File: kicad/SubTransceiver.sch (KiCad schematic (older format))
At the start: 50 parts

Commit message: Adding transceiver
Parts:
- U?: symbol RF_Mixer:ADE-6 -> RCTX-rescue:ADE-6-RF_Mixer
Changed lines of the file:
@@
 	1400 5050 1400 5150
 $Comp
-L RF_Mixer:ADE-6 U?
+L RCTX-rescue:ADE-6-RF_Mixer U?
 U 1 1 5FD5B378
 P 5100 4600

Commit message: New rx-tx bidirectional amplifier
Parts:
- removed C? (x6): 100p, symbol device:C
- removed C? (x4): 1u, symbol device:C
- removed D? (x4): D, symbol device:D
- removed L? (x7): L, symbol device:L
- removed R? (x4): R, symbol device:R
- removed U? (x2): MAX2650, smd-semi:SOT-143, symbol maxim_1:MAX2650
- removed U?: ADE-6, RF_Mini-Circuits:Mini-Circuits_CD542_LandPatternPL-052, symbol RCTX-rescue:ADE-6-RF_Mixer
- added C? (x12): 100p, symbol device:C
- added C? (x6): 1u, symbol device:C
- added L? (x4): L, symbol device:L
- added R? (x4): R, symbol device:R
- added U? (x4): MAR-6SM+, symbol mc-amplifiers:ERA-6+
- added U?: ADE-1+, RF_Mini-Circuits:Mini-Circuits_CD542_LandPatternPL-052, symbol RF_Mixer:ADE-1+
- added U? (x2): TLV70245_SOT23-5, TO_SOT_Packages_SMD:SOT-23-5, symbol regul:TLV70245_SOT23-5
- added U?: LM1117-3.3, symbol regul:LM1117-3.3
- added U? (x4): MAX2650, smd-semi:SOT-143, symbol maxim_1:MAX2650
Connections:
- net labels added: +VRx, +VTx, VCC
- net labels removed: RX_VCC, TX_VCC
- wire segments 127 -> 171
- no-connect marks 1 -> 0
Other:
- moved on the sheet: C?, J?, L?, U?, Y?

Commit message: New rx-tx bidirectional amplifier
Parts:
- removed C? (x16): 100p, symbol device:C
- removed C?: 100n, symbol device:C
- removed C? (x12): 1u, symbol device:C
- removed J?: 50 Ohm Antenna, symbol conn:Conn_Coaxial
- removed L? (x11): L, symbol device:L
- removed R? (x4): R, symbol device:R
- removed U?: Si4464, Package_DFN_QFN:QFN-20-1EP_4x4mm_P0.5mm_EP2.6x2.6mm_ThermalVias, symbol RF:Si4464
- removed U? (x4): MAR-6SM+, symbol mc-amplifiers:ERA-6+
- removed U?: ADE-1+, RF_Mini-Circuits:Mini-Circuits_CD542_LandPatternPL-052, symbol RF_Mixer:ADE-1+
- removed U? (x2): TLV70245_SOT23-5, TO_SOT_Packages_SMD:SOT-23-5, symbol regul:TLV70245_SOT23-5
- removed U?: LM1117-3.3, symbol regul:LM1117-3.3
- removed U? (x4): MAX2650, smd-semi:SOT-143, symbol maxim_1:MAX2650
- removed Y?: 30 MHz, symbol device:Crystal
- removed Y?: Si500D, Si500D, symbol Si500D:Si500D
- added C? (x16): 100p, symbol device:C
- added C?: 100n, symbol device:C
- added C? (x10): 1u, symbol device:C
- added J?: 50 Ohm Antenna, symbol conn:Conn_Coaxial
- added J?: TRANSCEIVER, symbol conn:Conn_01x06
- added L? (x8): L, symbol device:L
- added P?: TX_VCC, Connectors_Samtec:SL-102-X-XX_1x02, symbol RCTX-rescue:Conn_01x02-conn
- added P?: PWR_BUS, Connectors_Samtec:SL-104-X-XX_1x04, symbol RCTX-rescue:Conn_01x04-conn
- added R?: R, symbol device:R
- added U?: Si4464, Package_DFN_QFN:QFN-20-1EP_4x4mm_P0.5mm_EP2.6x2.6mm_ThermalVias, symbol RF:Si4464
- added U? (x2): TLV70245_SOT23-5, TO_SOT_Packages_SMD:SOT-23-5, symbol regul:TLV70245_SOT23-5
- added U? (x4): MAX2650, smd-semi:SOT-143, symbol maxim_1:MAX2650
- added U?: ADE-1+, RF_Mini-Circuits:Mini-Circuits_CD542_LandPatternPL-052, symbol RF_Mixer:ADE-1+
- added Y?: 30 MHz, symbol device:Crystal
- added Y?: Si500D, Si500D, symbol Si500D:Si500D
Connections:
- net labels removed: VCC
- wire segments 171 -> 178
- no-connect marks 0 -> 2
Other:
- note added: "+3.3V"
- note added: "+5V"
- note added: "/IRQ"
- note added: "/SEL"
- note added: "GND"
- note added: "Low pass filter fc: 260 MHz"
- note added: "Low pass filter fc: 80 MHz"
- note added: "PPM"
- note added: "SCLK"
- note added: "SDI"
- note added: "SDO"
- note added: "VBAT+"
- note added: "from Switches module (RF_SWITCH_3P2V)"
- note added: "to Switches module (RF_SWITCH_3P2V)"

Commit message: New rx-tx bidirectional amplifier
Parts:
- removed C? (x4): 100p, symbol device:C
- removed J?: TRANSCEIVER, symbol conn:Conn_01x06
- added C? (x3): 1u, symbol device:C
- added C? (x7): 100p, symbol device:C
- added J?: TRANSCEIVER, symbol conn:Conn_01x07
- added L?: L, symbol device:L
- added R?: R, symbol device:R
- Y?: value Si500D -> Si500DFAD165M000 / Si511NCB165M000C
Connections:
- wire segments 178 -> 204
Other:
- note added: "/RF_EN"
- note added: "Harmonic\ntermination"
- moved on the sheet: C?, J?, L?, P?, R?, U?, Y?

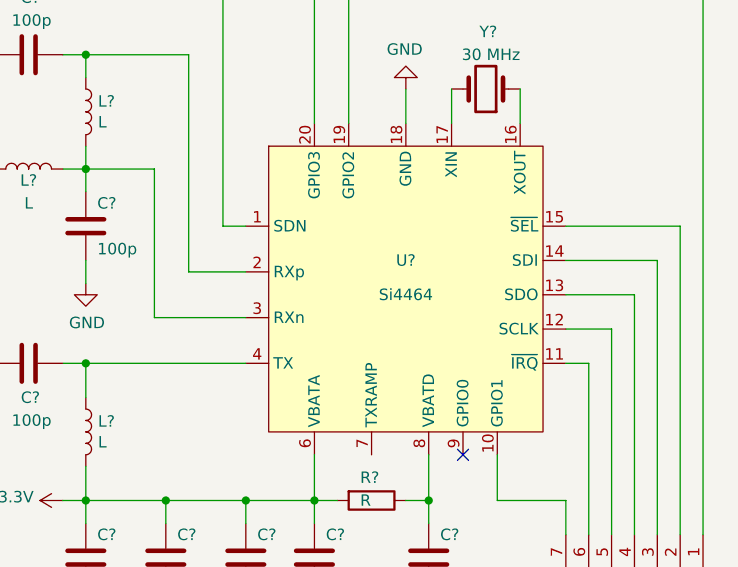
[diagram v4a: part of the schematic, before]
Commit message: Using ERF32FG12 SoC instead of PIC32MX
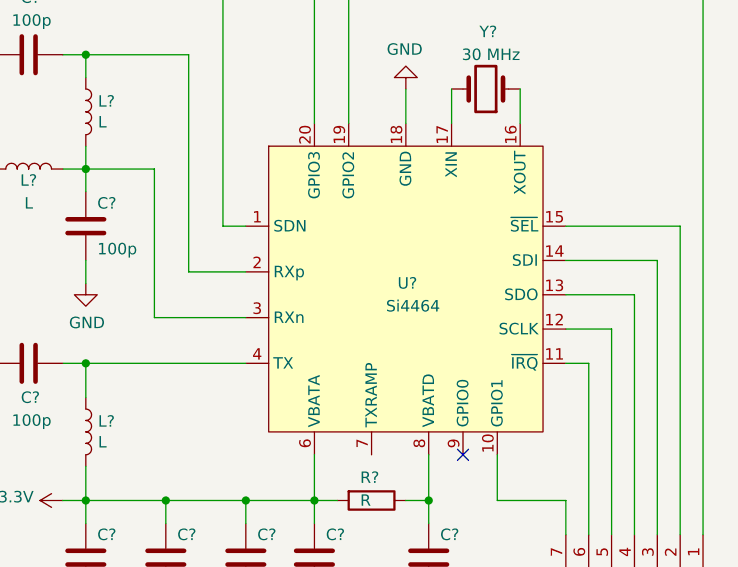
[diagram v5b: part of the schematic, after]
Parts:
- removed U?: Si4464, Package_DFN_QFN:QFN-20-1EP_4x4mm_P0.5mm_EP2.6x2.6mm_ThermalVias, symbol RF:Si4464
- added U?: Si4464, Package_DFN_QFN:QFN-20-1EP_4x4mm_P0.5mm_EP2.6x2.6mm_ThermalVias, symbol RF:Si4464
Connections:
- net +3V3: now also U?.6 (VBATA)
- net GND: now also U?.18 (GND), U?.21 (GND)
- net at C?.1, R?.1: now also U?.8 (VBATD)
- net at J?.1 (Pin_1), Y?.1 (OE): now also U?.1 (SDN)
- net at J?.7 (Pin_7): now also U?.10 (GPIO1)
- net at J?.6 (Pin_6): now also U?.11 (~IRQ)
- net at J?.5 (Pin_5): now also U?.12 (SCLK)
- net at J?.4 (Pin_4): now also U?.13 (SDO)
- net at J?.3 (Pin_3): now also U?.14 (SDI)
- net at J?.2 (Pin_2): now also U?.15 (~SEL)
- net at Y?.1: now also U?.16 (XOUT)
- net at Y?.2: now also U?.17 (XIN)
- net at U?.3 (EN): now also U?.19 (GPIO2)
- net at C?.2, L?.1: now also U?.2 (RXp)
- net at U?.3 (EN): now also U?.20 (GPIO3)
- net at C?.1, L?.2, L?.2: now also U?.3 (RXn)
- net at C?.2, L?.1: now also U?.4 (TX)
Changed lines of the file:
@@
 $Descr A4 11693 8268
 encoding utf-8
-Sheet 5 11
+Sheet 5 13
 Title ""
 Date ""
@@
 Wire Wire Line
 	9300 650  9300 1050
-$Comp
-L RF:Si4464 U?
-U 1 1 5FF51D98
-P 9700 4600
-F 0 "U?" H 9700 4750 50  0000 C CNN
-F 1 "Si4464" H 9700 4600 50  0000 C CNN
-F 2 "Package_DFN_QFN:QFN-20-1EP_4x4mm_P0.5mm_EP2.6x2.6mm_ThermalVias" H 9700 5800 50  0001 C CNN
-F 3 "https://www.silabs.com/documents/public/data-sheets/Si4464-63-61-60.pdf" H 9400 4500 50  0001 C CNN
-	1    9700 4600
-	1    0    0    -1
-$EndComp
 NoConn ~ 9950 5300
 Wire Wire Line
@@
 	4750 3750 4350 3750
 Connection ~ 8900 3050
+$Comp
+L RF:Si4464 U?
+U 1 1 5FEF1725
+P 9700 4600
+F 0 "U?" H 9750 4650 50  0000 R CNN
+F 1 "Si4464" H 9850 4550 50  0000 R CNN
+F 2 "Package_DFN_QFN:QFN-20-1EP_4x4mm_P0.5mm_EP2.6x2.6mm_ThermalVias" H 9700 5800 50  0001 C CNN
+F 3 "https://www.silabs.com/documents/public/data-sheets/Si4464-63-61-60.pdf" H 9800 4500 50  0001 C CNN
+	1    9700 4600
+	1    0    0    -1
+$EndComp
 $EndSCHEMATC
